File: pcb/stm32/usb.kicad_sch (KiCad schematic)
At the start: 0 parts

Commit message: Packages
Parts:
- added J16: USB_C_Receptacle, Connector_USB:USB_C_Receptacle_Amphenol_12401548E4-2A, symbol Connector:USB_C_Receptacle
- added U8: USBLC6-4SC6, Package_TO_SOT_SMD:SOT-23-6, symbol Power_Protection:USBLC6-4SC6
- added U9: CP2102N-Axx-xQFN24, Package_DFN_QFN:QFN-24-1EP_4x4mm_P0.5mm_EP2.6x2.6mm, symbol Interface_USB:CP2102N-Axx-xQFN24
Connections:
- new net: J16.A1 (GND), J16.A12 (GND), J16.B1 (GND), J16.B12 (GND)
- new net: J16.A4 (VBUS), J16.A9 (VBUS), J16.B4 (VBUS), J16.B9 (VBUS)
- new net: U9.2 (GND), U9.25 (GND)
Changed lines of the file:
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@@
     (effects (font (size 1.27 1.27) bold) (justify left))
   )
+  (symbol (lib_id "Power_Protection:USBLC6-4SC6") (at 52.07 76.2 0) (unit 1)
+    (in_bom yes) (on_board yes) (dnp no) (fields_autoplaced)
+    (property "Reference" "U8" (at 54.7117 64.77 0)
+      (effects (font (size 1.27 1.27)) (justify left))
+    )
+    (property "Value" "USBLC6-4SC6" (at 54.7117 67.31 0)
+      (effects (font (size 1.27 1.27)) (justify left))
+    )
+    (property "Footprint" "Package_TO_SOT_SMD:SOT-23-6" (at 52.07 88.9 0)
+      (effects (font (size 1.27 1.27)) hide)
+    )
+    (property "Datasheet" "https://www.st.com/resource/en/datasheet/usblc6-4.pdf" (at 57.15 67.31 0)
+      (effects (font (size 1.27 1.27)) hide)
+    )
+    (pin "1")
+    (pin "2")
+    (pin "3")
+    (pin "4")
+    (pin "5")
+    (pin "6")
+    (instances
+      (project "stm32"
+        (path "/cc56704c-71b4-401e-bec6-203f83946289/dd21196a-5f3f-4a2a-9bdd-afc183d705bd"
+          (reference "U8") (unit 1)
+        )
+      )
+    )
+  )
+  (symbol (lib_id "Connector:USB_C_Receptacle") (at 50.8 134.62 0) (unit 1)
+    (in_bom yes) (on_board yes) (dnp no) (fields_autoplaced)
+    (property "Reference" "J16" (at 50.8 102.87 0)
+      (effects (font (size 1.27 1.27)))
+    )
+    (property "Value" "USB_C_Receptacle" (at 50.8 105.41 0)
+      (effects (font (size 1.27 1.27)))
+    )
+    (property "Footprint" "Connector_USB:USB_C_Receptacle_Amphenol_12401548E4-2A" (at 54.61 134.62 0)
+      (effects (font (size 1.27 1.27)) hide)
+    )
+    (property "Datasheet" "https://www.usb.org/sites/default/files/documents/usb_type-c.zip" (at 54.61 134.62 0)
+      (effects (font (size 1.27 1.27)) hide)
+    )
+    (pin "A1")
+    (pin "A10")
+    (pin "A11")
+    (pin "A12")
+    (pin "A2")
+    (pin "A3")
+    (pin "A4")
+    (pin "A5")
+    (pin "A6")
+    (pin "A7")
+    (pin "A8")
+    (pin "A9")
+    (pin "B1")
+    (pin "B10")
+    (pin "B11")
+    (pin "B12")
+    (pin "B2")
+    (pin "B3")
+    (pin "B4")
+    (pin "B5")
+    (pin "B6")
+    (pin "B7")
+    (pin "B8")
+    (pin "B9")
+    (pin "S1")
+    (instances
+      (project "stm32"
+        (path "/cc56704c-71b4-401e-bec6-203f83946289/dd21196a-5f3f-4a2a-9bdd-afc183d705bd"
+          (reference "J16") (unit 1)
+        )
+      )
+    )
+  )
+  (symbol (lib_id "Interface_USB:CP2102N-Axx-xQFN24") (at 97.79 77.47 0) (unit 1)
+    (in_bom yes) (on_board yes) (dnp no) (fields_autoplaced)
+    (property "Reference" "U9" (at 99.7459 105.41 0)
+      (effects (font (size 1.27 1.27)) (justify left))
+    )
+    (property "Value" "CP2102N-Axx-xQFN24" (at 99.7459 107.95 0)
+      (effects (font (size 1.27 1.27)) (justify left))
+    )
+    (property "Footprint" "Package_DFN_QFN:QFN-24-1EP_4x4mm_P0.5mm_EP2.6x2.6mm" (at 129.54 104.14 0)
+      (effects (font (size 1.27 1.27)) hide)
+    )
+    (property "Datasheet" "https://www.silabs.com/documents/public/data-sheets/cp2102n-datasheet.pdf" (at 99.06 96.52 0)
+      (effects (font (size 1.27 1.27)) hide)
+    )
+    (pin "1")
+    (pin "10")
+    (pin "11")
+    (pin "12")
+    (pin "13")
+    (pin "14")
+    (pin "15")
+    (pin "16")
+    (pin "17")
+    (pin "18")
+    (pin "19")
+    (pin "2")
+    (pin "20")
+    (pin "21")
+    (pin "22")
+    (pin "23")
+    (pin "24")
+    (pin "25")
+    (pin "3")
+    (pin "4")
+    (pin "5")
+    (pin "6")
+    (pin "7")
+    (pin "8")
+    (pin "9")
+    (instances
+      (project "stm32"
+        (path "/cc56704c-71b4-401e-bec6-203f83946289/dd21196a-5f3f-4a2a-9bdd-afc183d705bd"
+          (reference "U9") (unit 1)
+        )
+      )
+    )
+  )
 )

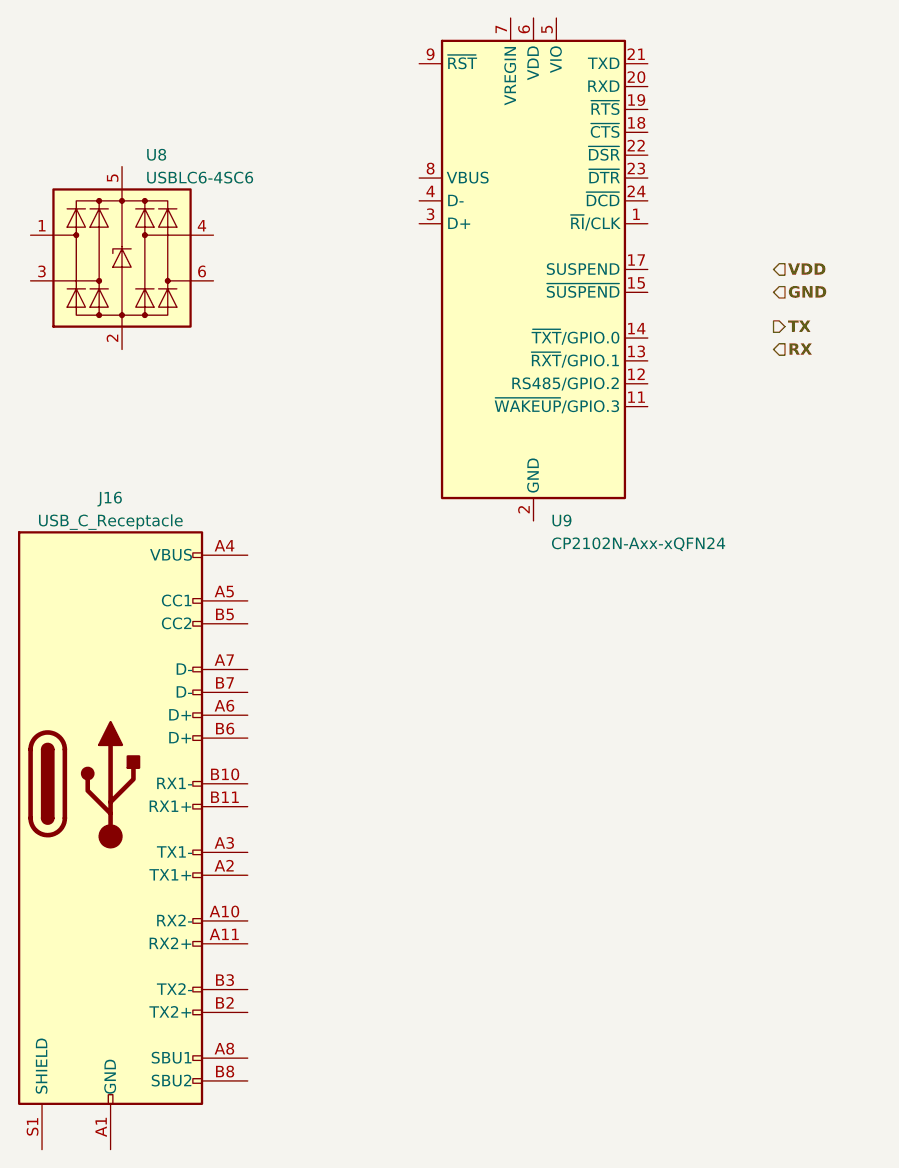
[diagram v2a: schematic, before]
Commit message: VDD supply added
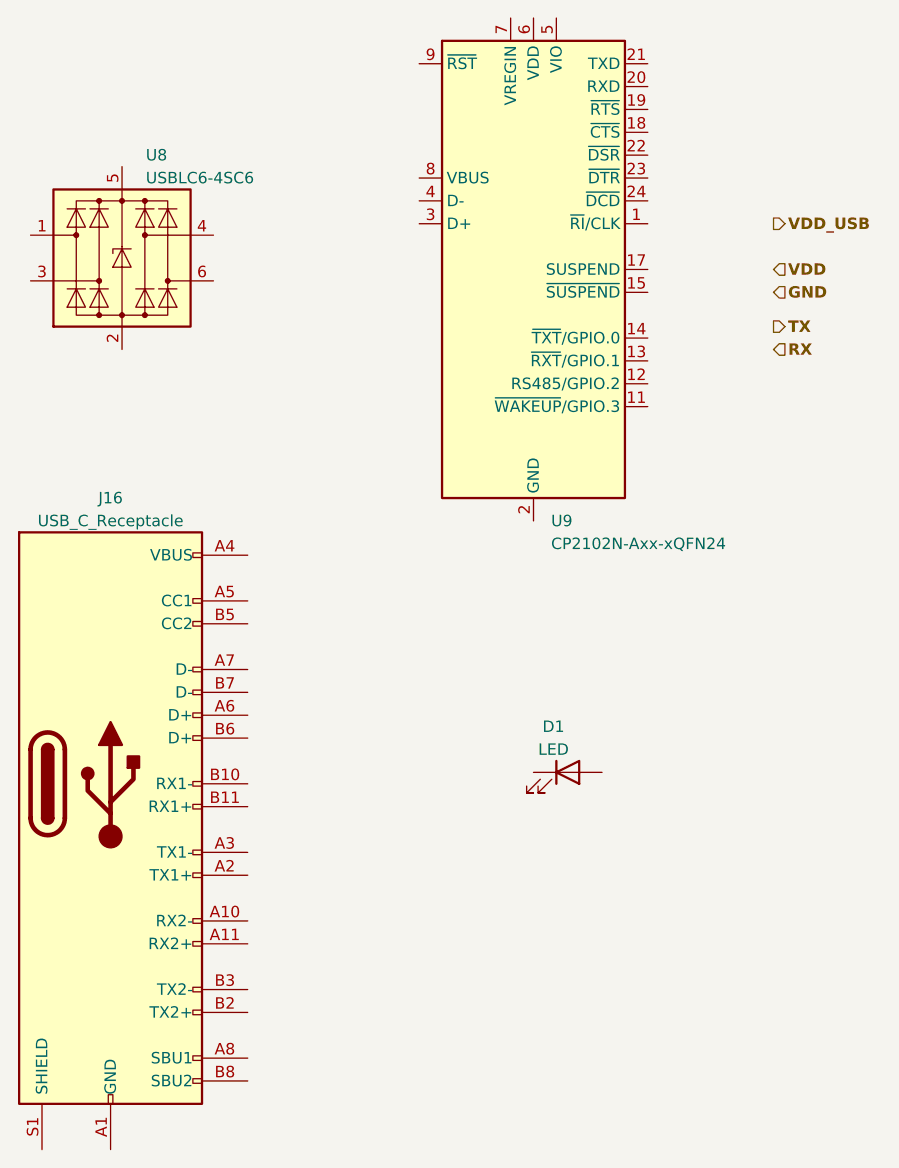
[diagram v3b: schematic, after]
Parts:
- added D1: LED, symbol Device:LED
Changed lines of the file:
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@@
     (effects (font (size 1.27 1.27) bold) (justify left))
+  )
+  (hierarchical_label "VDD_USB" (shape output) (at 124.46 72.39 0) (fields_autoplaced)
+    (effects (font (size 1.27 1.27) (thickness 0.254) bold) (justify left))
   )
   (hierarchical_label "VDD" (shape input) (at 124.46 77.47 0) (fields_autoplaced)
@@
     (effects (font (size 1.27 1.27) bold) (justify left))
   )
+  (symbol (lib_id "Device:LED") (at 101.6 133.35 0) (unit 1)
+    (in_bom yes) (on_board yes) (dnp no) (fields_autoplaced)
+    (property "Reference" "D1" (at 100.0125 128.27 0)
+      (effects (font (size 1.27 1.27)))
+    )
+    (property "Value" "LED" (at 100.0125 130.81 0)
+      (effects (font (size 1.27 1.27)))
+    )
+    (property "Footprint" "" (at 101.6 133.35 0)
+      (effects (font (size 1.27 1.27)) hide)
+    )
+    (property "Datasheet" "~" (at 101.6 133.35 0)
+      (effects (font (size 1.27 1.27)) hide)
+    )
+    (pin "1")
+    (pin "2")
+    (instances
+      (project "stm32"
+        (path "/cc56704c-71b4-401e-bec6-203f83946289/dd21196a-5f3f-4a2a-9bdd-afc183d705bd"
+          (reference "D1") (unit 1)
+        )
+      )
+    )
+  )
   (symbol (lib_id "Power_Protection:USBLC6-4SC6") (at 52.07 76.2 0) (unit 1)

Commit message: Small work on pcb
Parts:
- added D2: ???, Diode_SMD:D_SOD-323, symbol Diode:SD05_SOD323
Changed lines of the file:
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@@
+    )
+  )
+  (symbol (lib_id "Diode:SD05_SOD323") (at 95.25 148.59 90) (unit 1)
+    (in_bom yes) (on_board yes) (dnp no) (fields_autoplaced)
+    (property "Reference" "D2" (at 97.79 147.955 90)
+      (effects (font (size 1.27 1.27)) (justify right))
+    )
+    (property "Value" "???" (at 97.79 150.495 90)
+      (effects (font (size 1.27 1.27)) (justify right))
+    )
+    (property "Footprint" "Diode_SMD:D_SOD-323" (at 100.33 148.59 0)
+      (effects (font (size 1.27 1.27)) hide)
+    )
+    (property "Datasheet" "https://www.littelfuse.com/~/media/electronics/datasheets/tvs_diode_arrays/littelfuse_tvs_diode_array_sd_c_datasheet.pdf.pdf" (at 95.25 148.59 0)
+      (effects (font (size 1.27 1.27)) hide)
+    )
+    (pin "1")
+    (pin "2")
+    (instances
+      (project "stm32"
+        (path "/cc56704c-71b4-401e-bec6-203f83946289/8878edf1-eecf-4d8b-8425-07bf183b31b3"
+          (reference "D2") (unit 1)
+        )
+        (path "/cc56704c-71b4-401e-bec6-203f83946289/dd21196a-5f3f-4a2a-9bdd-afc183d705bd"
+          (reference "D3") (unit 1)
+        )
+      )
     )
   )
